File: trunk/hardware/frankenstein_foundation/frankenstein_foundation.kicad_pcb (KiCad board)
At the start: 2 copper layers, 100 x 99.9 mm, 4 parts, among them P1 CONN_4X2, P2 CONN_10X2, P3 CONN_2, P4 CONN_5X2

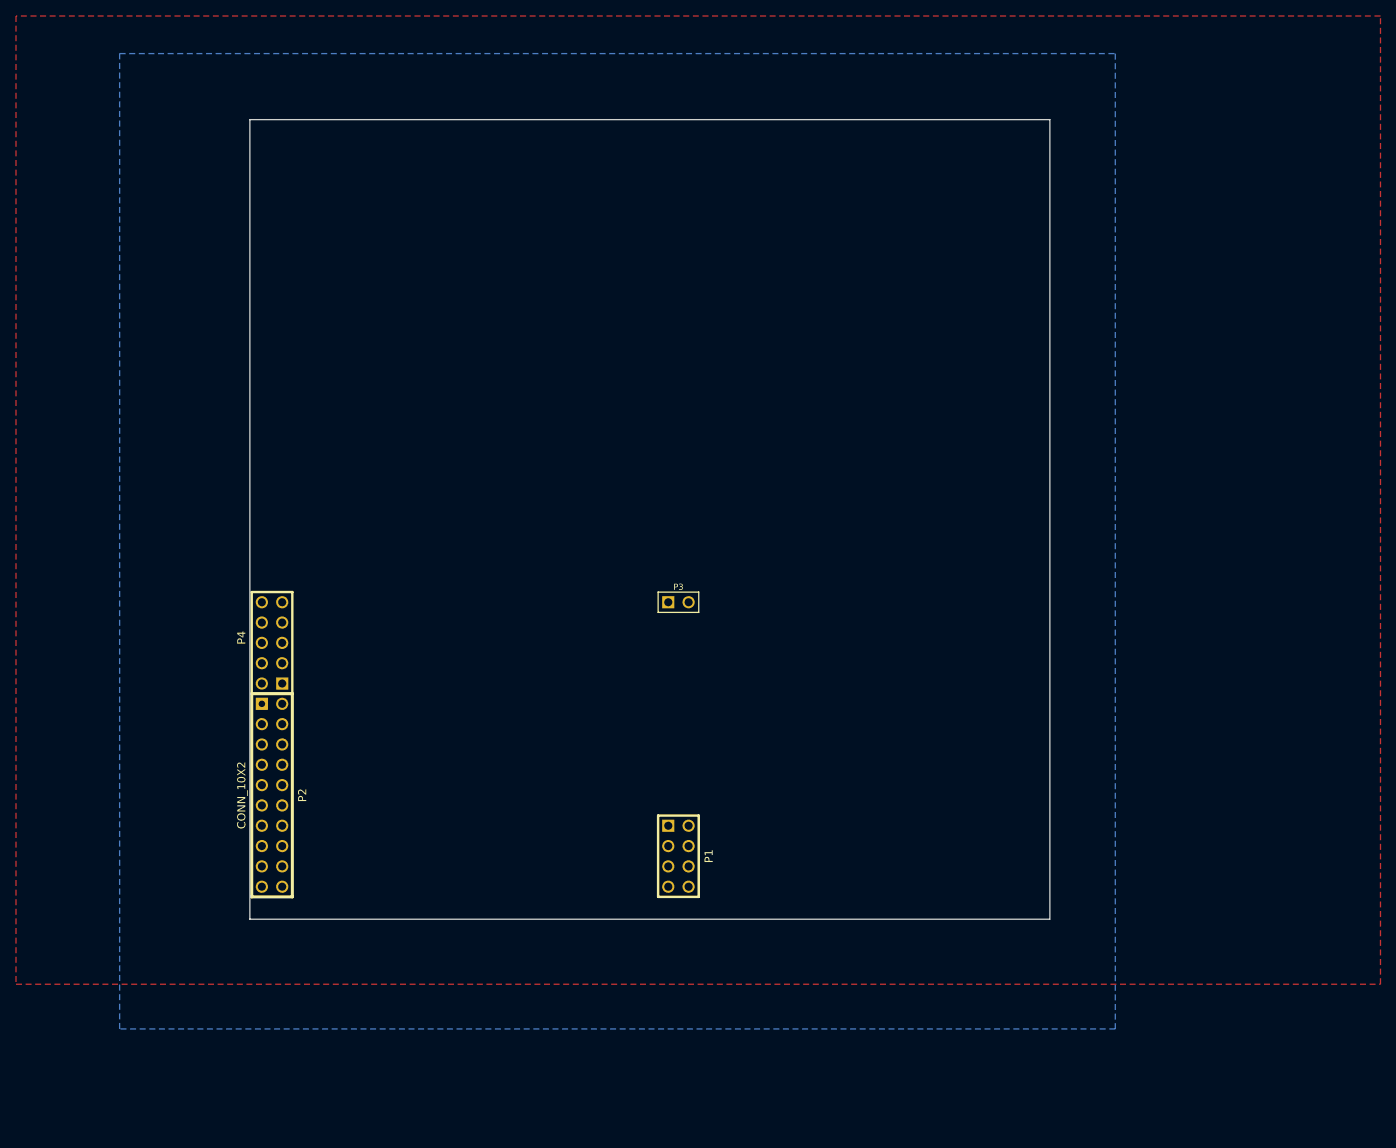
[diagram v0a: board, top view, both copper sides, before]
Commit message: some track improvements
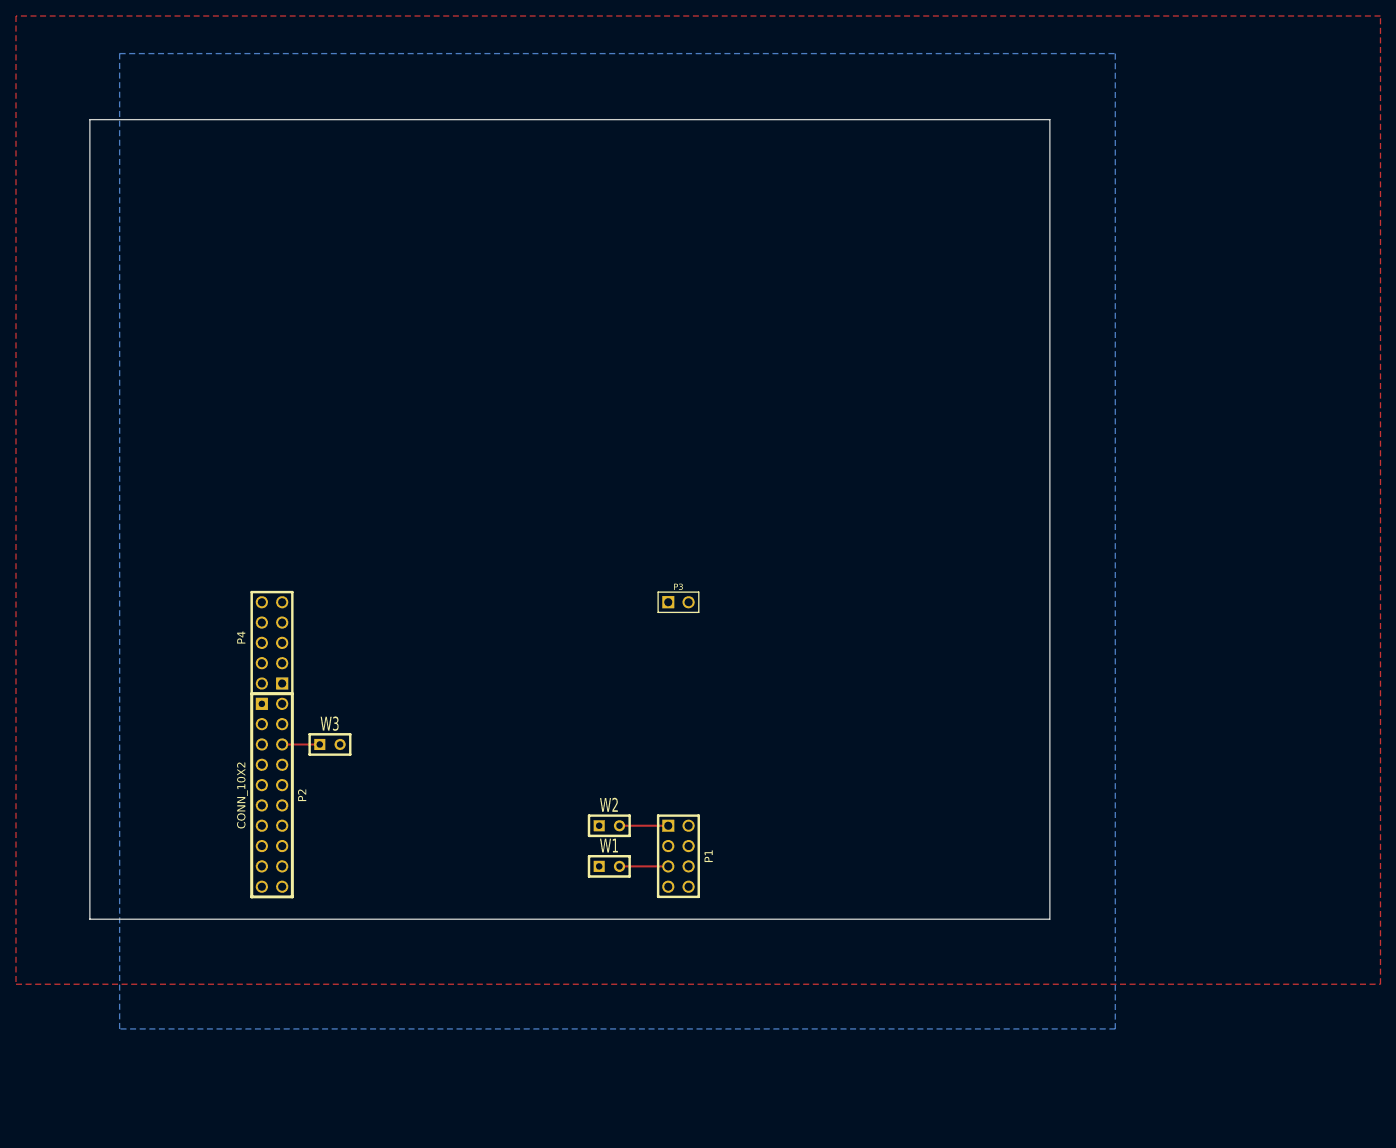
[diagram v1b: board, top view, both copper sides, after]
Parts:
- added W1: TEST, SIL-2, F.Cu at (170.4, 185.4)
- added W2: TEST, SIL-2, F.Cu at (170.4, 180.3)
- added W3: TEST, SIL-2, F.Cu at (135.5, 170.2)
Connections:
- P1 pad 1: (no net) -> /PA8
- P1 pad 5: (no net) -> /PC6
- P2 pad 6: (no net) -> CAN_RX
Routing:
- net /PC6: track 0.00 -> 6.10 mm
- net /PA8: track 0.00 -> 6.10 mm
- net CAN_RX: track 0.00 -> 4.70 mm
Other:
- board size 100 x 99.9 mm -> 120 x 99.9 mm
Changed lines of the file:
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@@
 (kicad_pcb (version 3) (host pcbnew "(2013-07-07 BZR 4022)-stable")
   (general
-    (links 3)
-    (no_connects 0)
+    (links 7)
+    (no_connects 1)
     (area 96.266 79.121 266.827001 205.740001)
     (thickness 1.6)
     (drawings 16)
-    (tracks 0)
+    (tracks 3)
     (zones 0)
-    (modules 4)
-    (nets 2)
+    (modules 7)
+    (nets 5)
   )
   (page A3)
@@
   )
   (net 0 "")
-  (net 1 GND)
+  (net 1 /PA8)
+  (net 2 /PC6)
+  (net 3 CAN_RX)
+  (net 4 GND)
   (net_class Default "This is the default net class."
     (clearance 0.2032)
@@
     (uvia_drill 0.127)
     (add_net "")
+    (add_net /PA8)
+    (add_net /PC6)
+    (add_net CAN_RX)
     (add_net GND)
   )
@@
     (pad 1 thru_hole rect (at -3.81 1.27 270) (size 1.524 1.524) (drill 1.016)
       (layers *.Cu *.Mask F.SilkS)
+      (net 1 /PA8)
     )
     (pad 2 thru_hole circle (at -3.81 -1.27 270) (size 1.524 1.524) (drill 1.016)
@@
     (pad 5 thru_hole circle (at 1.27 1.27 270) (size 1.524 1.524) (drill 1.016)
       (layers *.Cu *.Mask F.SilkS)
+      (net 2 /PC6)
     )
     (pad 6 thru_hole circle (at 1.27 -1.27 270) (size 1.524 1.524) (drill 1.016)
@@
     (pad 7 thru_hole circle (at 3.81 1.27 270) (size 1.524 1.524) (drill 1.016)
       (layers *.Cu *.Mask F.SilkS)
-      (net 1 GND)
+      (net 4 GND)
     )
     (pad 8 thru_hole circle (at 3.81 -1.27 270) (size 1.524 1.524) (drill 1.016)
       (layers *.Cu *.Mask F.SilkS)
-      (net 1 GND)
+      (net 4 GND)
     )
     (model pin_array/pins_array_4x2.wrl
@@
     (pad 6 thru_hole circle (at -6.35 -1.27 270) (size 1.524 1.524) (drill 1.016)
       (layers *.Cu *.Mask F.SilkS)
+      (net 3 CAN_RX)
     )
     (pad 7 thru_hole circle (at -3.81 1.27 270) (size 1.524 1.524) (drill 1.016)
@@
     (pad 19 thru_hole circle (at 11.43 1.27 270) (size 1.524 1.524) (drill 1.016)
       (layers *.Cu *.Mask F.SilkS)
-      (net 1 GND)
+      (net 4 GND)
     )
     (pad 20 thru_hole circle (at 11.43 -1.27 270) (size 1.524 1.524) (drill 1.016)
       (layers *.Cu *.Mask F.SilkS)
-      (net 1 GND)
+      (net 4 GND)
     )
     (model pin_array/pins_array_12x2.wrl
@@
     )
   )
-  (gr_line (start 225.5 192.024) (end 125.5 192.024) (angle 90) (layer Edge.Cuts) (width 0.1))
+  (module SIL-2 (layer F.Cu)
+    (at 170.434 185.42)
+    (descr "Connecteurs 2 pins")
+    (tags "CONN DEV")
+    (fp_text reference W1 (at 0 -2.54) (layer F.SilkS)
+      (effects (font (size 1.72974 1.08712) (thickness 0.3048)))
+    )
+    (fp_text value TEST (at 0 -2.54) (layer F.SilkS) hide
+      (effects (font (size 1.524 1.016) (thickness 0.3048)))
+    )
+    (fp_line (start -2.54 1.27) (end -2.54 -1.27) (layer F.SilkS) (width 0.3048))
+    (fp_line (start -2.54 -1.27) (end 2.54 -1.27) (layer F.SilkS) (width 0.3048))
+    (fp_line (start 2.54 -1.27) (end 2.54 1.27) (layer F.SilkS) (width 0.3048))
+    (fp_line (start 2.54 1.27) (end -2.54 1.27) (layer F.SilkS) (width 0.3048))
+    (pad 1 thru_hole rect (at -1.27 0) (size 1.397 1.397) (drill 0.8128)
+      (layers *.Cu *.Mask F.SilkS)
+    )
+    (pad 2 thru_hole circle (at 1.27 0) (size 1.397 1.397) (drill 0.8128)
+      (layers *.Cu *.Mask F.SilkS)
+      (net 2 /PC6)
+    )
+  )
+  (module SIL-2 (layer F.Cu)
+    (at 170.434 180.34)
+    (descr "Connecteurs 2 pins")
+    (tags "CONN DEV")
+    (fp_text reference W2 (at 0 -2.54) (layer F.SilkS)
+      (effects (font (size 1.72974 1.08712) (thickness 0.3048)))
+    )
+    (fp_text value TEST (at 0 -2.54) (layer F.SilkS) hide
+      (effects (font (size 1.524 1.016) (thickness 0.3048)))
+    )
+    (fp_line (start -2.54 1.27) (end -2.54 -1.27) (layer F.SilkS) (width 0.3048))
+    (fp_line (start -2.54 -1.27) (end 2.54 -1.27) (layer F.SilkS) (width 0.3048))
+    (fp_line (start 2.54 -1.27) (end 2.54 1.27) (layer F.SilkS) (width 0.3048))
+    (fp_line (start 2.54 1.27) (end -2.54 1.27) (layer F.SilkS) (width 0.3048))
+    (pad 1 thru_hole rect (at -1.27 0) (size 1.397 1.397) (drill 0.8128)
+      (layers *.Cu *.Mask F.SilkS)
+    )
+    (pad 2 thru_hole circle (at 1.27 0) (size 1.397 1.397) (drill 0.8128)
+      (layers *.Cu *.Mask F.SilkS)
+      (net 1 /PA8)
+    )
+  )
+  (module SIL-2 (layer F.Cu)
+    (at 135.509 170.18)
+    (descr "Connecteurs 2 pins")
+    (tags "CONN DEV")
+    (fp_text reference W3 (at 0 -2.54) (layer F.SilkS)
+      (effects (font (size 1.72974 1.08712) (thickness 0.3048)))
+    )
+    (fp_text value TEST (at 0 -2.54) (layer F.SilkS) hide
+      (effects (font (size 1.524 1.016) (thickness 0.3048)))
+    )
+    (fp_line (start -2.54 1.27) (end -2.54 -1.27) (layer F.SilkS) (width 0.3048))
+    (fp_line (start -2.54 -1.27) (end 2.54 -1.27) (layer F.SilkS) (width 0.3048))
+    (fp_line (start 2.54 -1.27) (end 2.54 1.27) (layer F.SilkS) (width 0.3048))
+    (fp_line (start 2.54 1.27) (end -2.54 1.27) (layer F.SilkS) (width 0.3048))
+    (pad 1 thru_hole rect (at -1.27 0) (size 1.397 1.397) (drill 0.8128)
+      (layers *.Cu *.Mask F.SilkS)
+      (net 3 CAN_RX)
+    )
+    (pad 2 thru_hole circle (at 1.27 0) (size 1.397 1.397) (drill 0.8128)
+      (layers *.Cu *.Mask F.SilkS)
+      (net 3 CAN_RX)
+    )
+  )
+  (gr_line (start 225.5 192.024) (end 105.5 192.024) (angle 90) (layer Edge.Cuts) (width 0.1))
   (gr_line (start 225.5 92.075) (end 225.5 192.024) (angle 90) (layer Edge.Cuts) (width 0.1))
-  (gr_line (start 125.5 192.024) (end 125.5 92.075) (angle 90) (layer Edge.Cuts) (width 0.1))
-  (gr_line (start 125.5 92.075) (end 225.5 92.075) (angle 90) (layer Edge.Cuts) (width 0.1))
+  (gr_line (start 105.5 192.024) (end 105.5 92.075) (angle 90) (layer Edge.Cuts) (width 0.1))
+  (gr_line (start 105.5 92.075) (end 225.5 92.075) (angle 90) (layer Edge.Cuts) (width 0.1))
   (gr_line (start 120.65 93.345) (end 186.69 93.345) (angle 90) (layer Cmts.User) (width 0.2))
   (gr_line (start 186.69 190.5) (end 186.69 93.472) (angle 90) (layer Cmts.User) (width 0.2))
@@
   (gr_line (start 127 187.96) (end 129.54 187.96) (angle 90) (layer Cmts.User) (width 0.2))
   (gr_line (start 127 127) (end 127 187.96) (angle 90) (layer Cmts.User) (width 0.2))
-  (zone (net 1) (net_name GND) (layer F.Cu) (hatch edge 0.508)
+  (segment (start 171.704 180.34) (end 177.8 180.34) (width 0.254) (layer F.Cu) (net 1))
+  (segment (start 171.704 185.42) (end 177.8 185.42) (width 0.254) (layer F.Cu) (net 2))
+  (segment (start 134.239 170.18) (end 129.54 170.18) (width 0.254) (layer F.Cu) (net 3))
+  (zone (net 4) (net_name GND) (layer F.Cu) (hatch edge 0.508)
     (connect_pads (clearance 0.254))
     (min_thickness 0.254)
@@
     )
   )
-  (zone (net 1) (net_name GND) (layer B.Cu) (hatch edge 0.508)
+  (zone (net 4) (net_name GND) (layer B.Cu) (hatch edge 0.508)
     (connect_pads (clearance 0.254))
     (min_thickness 0.254)

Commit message: 
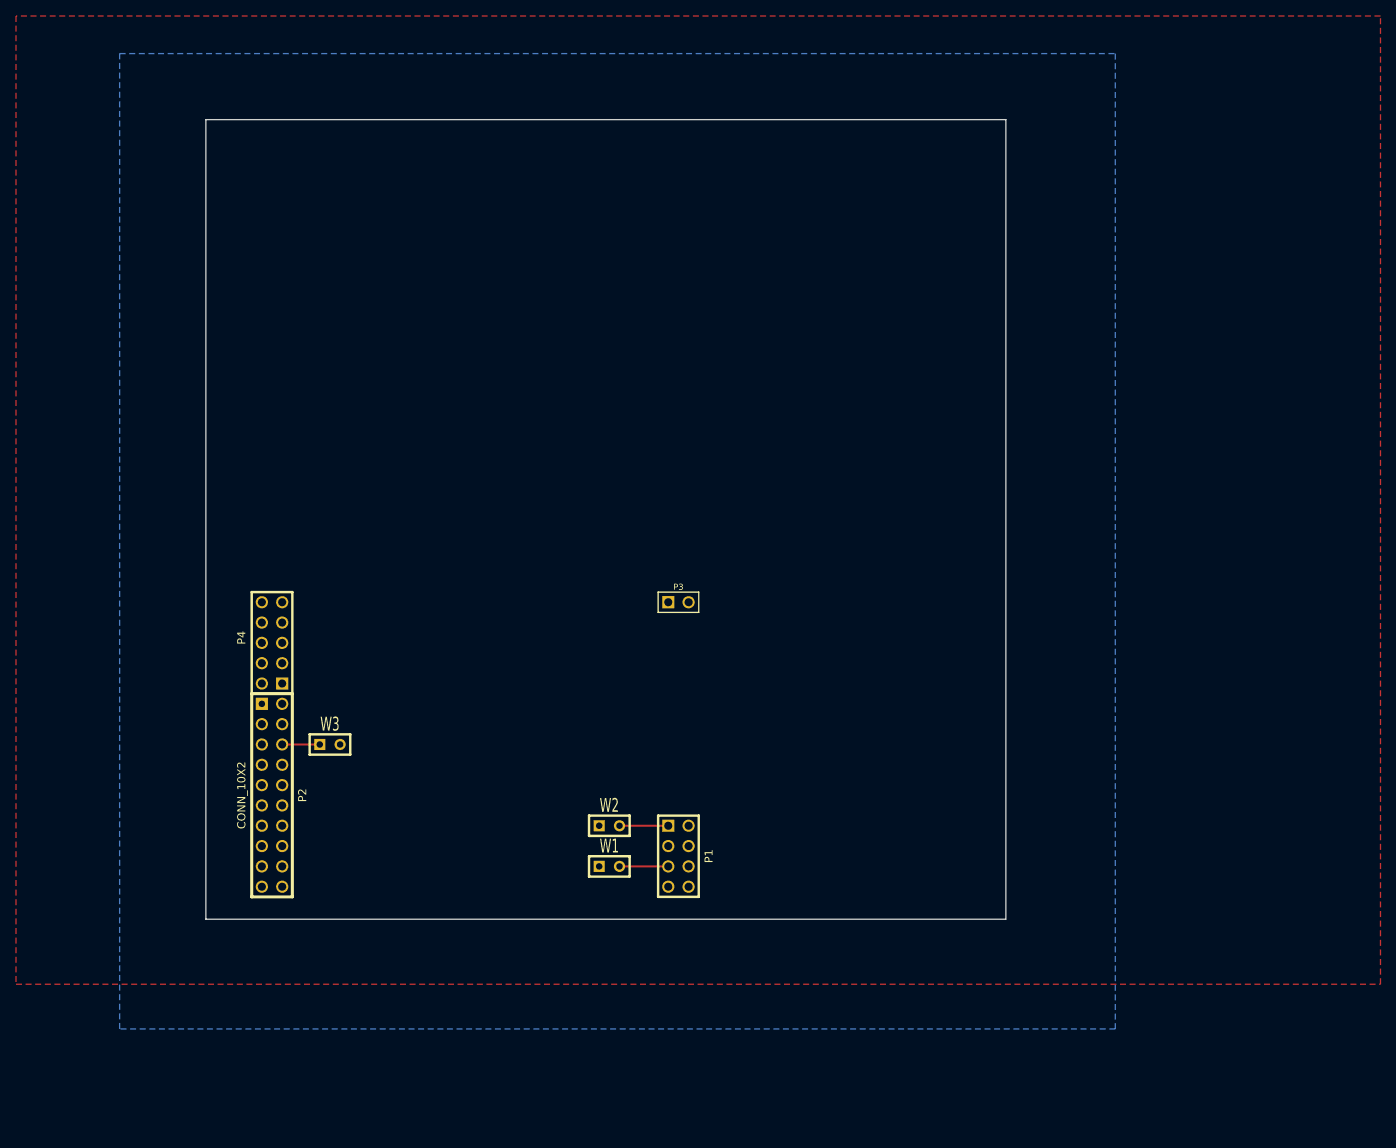
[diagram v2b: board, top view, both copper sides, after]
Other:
- board size 120 x 99.9 mm -> 100 x 99.9 mm
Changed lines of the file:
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@@
     )
   )
-  (gr_line (start 225.5 192.024) (end 105.5 192.024) (angle 90) (layer Edge.Cuts) (width 0.1))
-  (gr_line (start 225.5 92.075) (end 225.5 192.024) (angle 90) (layer Edge.Cuts) (width 0.1))
-  (gr_line (start 105.5 192.024) (end 105.5 92.075) (angle 90) (layer Edge.Cuts) (width 0.1))
-  (gr_line (start 105.5 92.075) (end 225.5 92.075) (angle 90) (layer Edge.Cuts) (width 0.1))
+  (gr_line (start 220 192.024) (end 120 192.024) (angle 90) (layer Edge.Cuts) (width 0.1))
+  (gr_line (start 220 92.075) (end 220 192.024) (angle 90) (layer Edge.Cuts) (width 0.1))
+  (gr_line (start 120 192.024) (end 120 92.075) (angle 90) (layer Edge.Cuts) (width 0.1))
+  (gr_line (start 120 92.075) (end 220 92.075) (angle 90) (layer Edge.Cuts) (width 0.1))
   (gr_line (start 120.65 93.345) (end 186.69 93.345) (angle 90) (layer Cmts.User) (width 0.2))
   (gr_line (start 186.69 190.5) (end 186.69 93.472) (angle 90) (layer Cmts.User) (width 0.2))
